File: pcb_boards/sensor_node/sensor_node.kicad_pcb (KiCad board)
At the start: 2 copper layers, 93 x 93 mm, 61 parts, among them IC1 PCF2129AT, J2 Conn_02x03_Odd_Even, J3 USB_B_Micro, U1 SiP32431, U2 ESP32-WROOM-32, U3 RF-LORA-868-SO, U7 RP604x, U8 SiP32431

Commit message: Merge with local version. Bug fixes and node improvements.
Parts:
- IC1: value PCF2129AT -> PCF2129T
- moved I2C2 1.00 mm to (67.5, 124.5)
- moved I2C3 1.00 mm to (102.5, 124.5)
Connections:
- net /~RST renamed /~{RST}
- net /~RST_I2C renamed /~{RST_I2C}
- net /~RST_RF renamed /~{RST_RF}
- IC1 pad 10: Net-(IC1-Pad10) -> unconnected-(IC1-Pad10)
- IC1 pad 11: Net-(IC1-Pad11) -> unconnected-(IC1-Pad11)
- IC1 pad 12: Net-(IC1-Pad12) -> unconnected-(IC1-Pad12)
- IC1 pad 13: Net-(IC1-Pad13) -> unconnected-(IC1-Pad13)
- IC1 pad 14: Net-(IC1-Pad14) -> unconnected-(IC1-Pad14)
- IC1 pad 15: Net-(IC1-Pad15) -> unconnected-(IC1-Pad15)
- IC1 pad 16: Net-(IC1-Pad16) -> unconnected-(IC1-Pad16)
- IC1 pad 3: Net-(IC1-Pad3) -> unconnected-(IC1-Pad3)
- IC1 pad 6: Net-(IC1-Pad6) -> unconnected-(IC1-Pad6)
- IC1 pad 7: Net-(IC1-Pad7) -> unconnected-(IC1-Pad7)
- IC1 pad 9: Net-(IC1-Pad9) -> unconnected-(IC1-Pad9)
- J3 pad 4: Net-(J3-Pad4) -> unconnected-(J3-Pad4)
- U1 pad 6: Net-(U1-Pad6) -> unconnected-(U1-Pad6)
- U2 pad 13: Net-(U2-Pad13) -> unconnected-(U2-Pad13)
- U2 pad 14: Net-(U2-Pad14) -> unconnected-(U2-Pad14)
- U2 pad 17: Net-(U2-Pad17) -> unconnected-(U2-Pad17)
- U2 pad 18: Net-(U2-Pad18) -> unconnected-(U2-Pad18)
- U2 pad 19: Net-(U2-Pad19) -> unconnected-(U2-Pad19)
- U2 pad 20: Net-(U2-Pad20) -> unconnected-(U2-Pad20)
- U2 pad 21: Net-(U2-Pad21) -> unconnected-(U2-Pad21)
- U2 pad 22: Net-(U2-Pad22) -> unconnected-(U2-Pad22)
- U2 pad 23: Net-(U2-Pad23) -> unconnected-(U2-Pad23)
- U2 pad 29: Net-(U2-Pad29) -> unconnected-(U2-Pad29)
- U2 pad 32: Net-(U2-Pad32) -> unconnected-(U2-Pad32)
- U3 pad 10: Net-(U3-Pad10) -> unconnected-(U3-Pad10)
- U3 pad 11: Net-(U3-Pad11) -> unconnected-(U3-Pad11)
- U3 pad 8: Net-(U3-Pad8) -> unconnected-(U3-Pad8)
- U3 pad 9: Net-(U3-Pad9) -> unconnected-(U3-Pad9)
- U8 pad 6: Net-(U8-Pad6) -> unconnected-(U8-Pad6)
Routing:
- net /SCL: track 163.8 -> 162.1 mm
- net /~{RST}: track 36.3 -> 37.6 mm
- net /SDA: track 144.9 -> 143.6 mm
- net /~{RST_I2C}: track 132.4 -> 131.7 mm
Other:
- net class Default removed
- net class Power removed
- board text added: "MIRRA"
- board text added: "RST"
- board text added: "Rev. 6"
- board text added: "~{RST}"
- board text removed: "GEMS"
- board text removed: "Rev. 5"
- board text removed: "~RST"

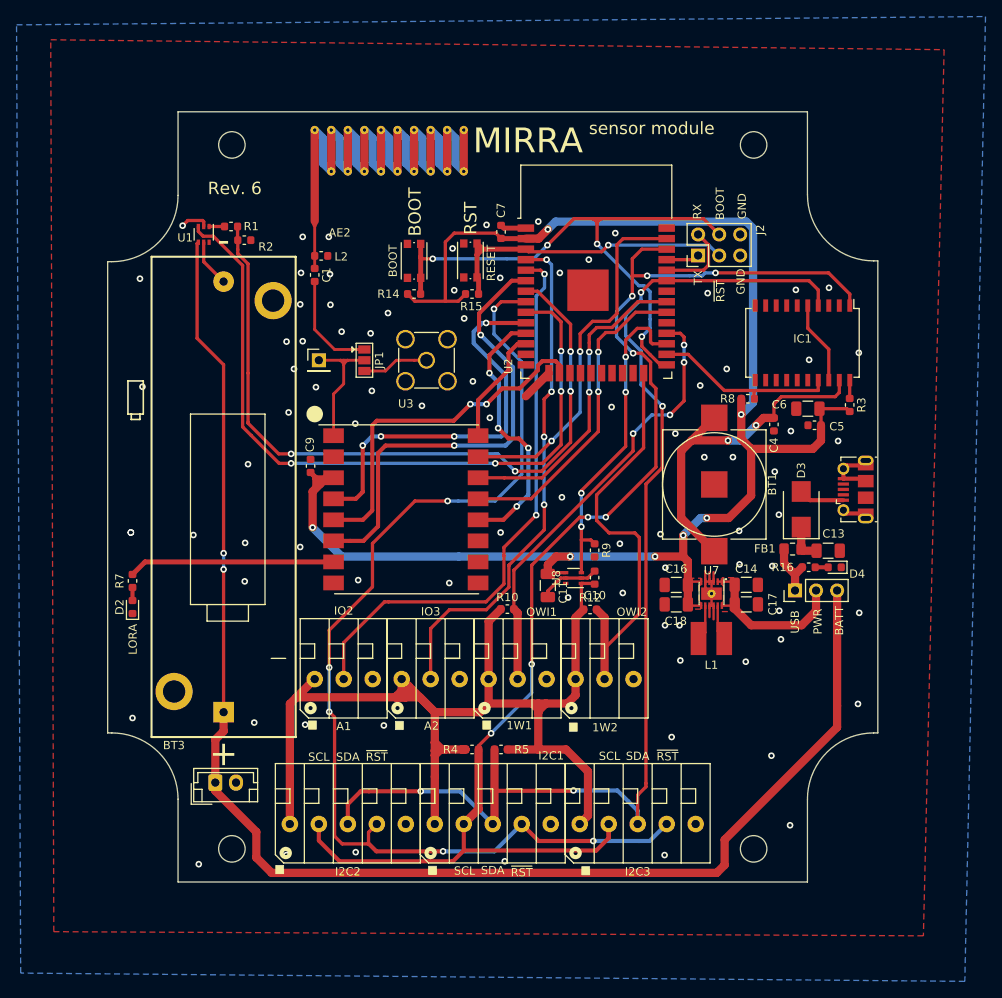
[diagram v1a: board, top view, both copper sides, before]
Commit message: New PDB version.
sensor node: added FTDI chip for USB comms
sensor node: implemented page feedback
sensor node: remove aerial, and SMA connector, update interfacing and RTC

sensor hat: update to two PCBs for reduced thermal conductivity
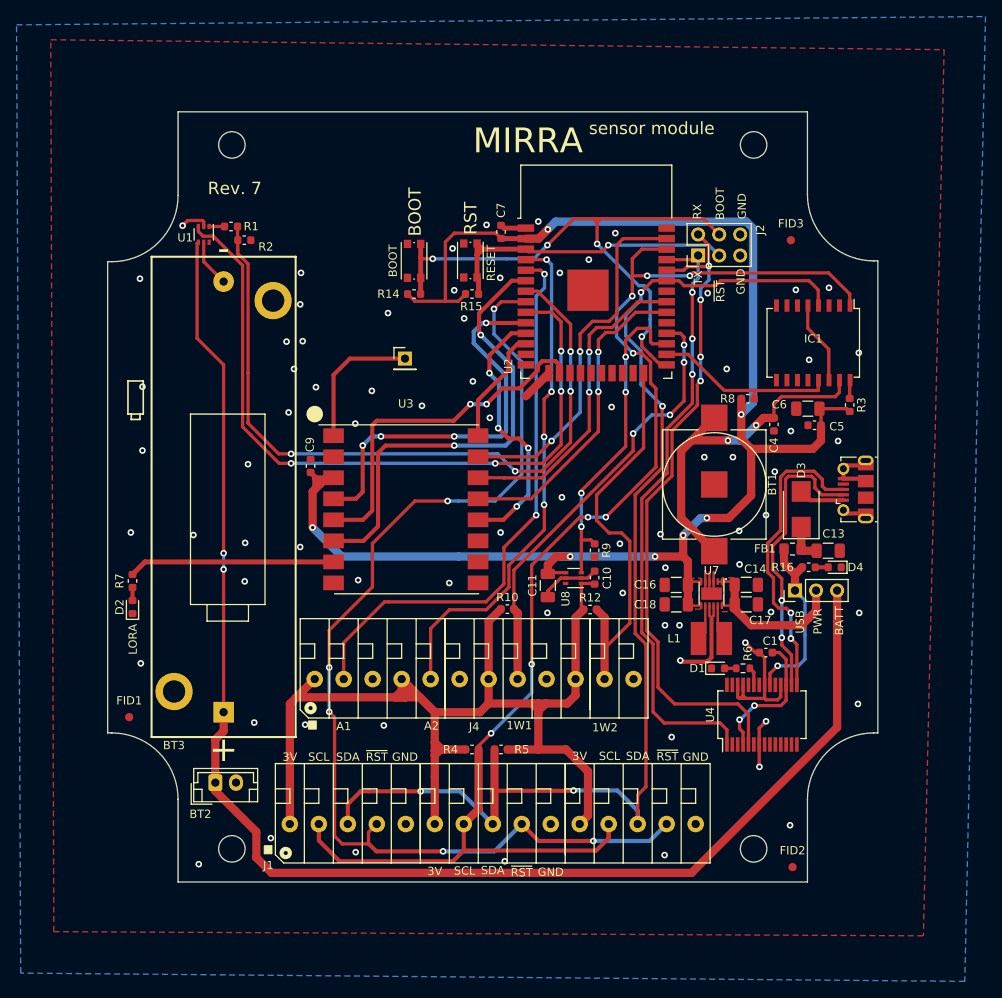
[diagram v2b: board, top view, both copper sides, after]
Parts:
- removed AE2: Antenna, RF_Antenna:Texas_SWRA416_868MHz_915MHz
- removed ANT1: Conn_Coaxial, Connector_Coaxial:SMA_Amphenol_901-144_Vertical
- removed I2C1, I2C2, I2C3: Conn_01x05, gems_footprints:TerminalBlock_Phoenix_PTSA-1,2-2-3,5-F-THR-1x05-P3.50mm_45Degree
- removed IO2, IO3, OWI1, OWI2: Conn_01x03, gems_footprints:TerminalBlock_Phoenix_PTSA-1,2-2-3,5-F-THR-1x03-P3.50mm_45Degree
- removed JP1: Jumper_3_Open, Jumper:SolderJumper-3_P1.3mm_Open_Pad1.0x1.5mm
- removed L2: 12nH, Inductor_SMD:L_0603_1608Metric
- added D1: LED, LED_SMD:LED_0603_1608Metric, F.Cu at (112.2, 105.7)
- added FID1: Fiducial, Fiducial:Fiducial_1mm_Mask2mm, F.Cu at (41.1, 111.6)
- added FID2: Fiducial, Fiducial:Fiducial_1mm_Mask2mm, F.Cu at (121.2, 129.7)
- added FID3: Fiducial, Fiducial:Fiducial_1mm_Mask2mm, F.Cu at (121.0, 54.0)
- added J1: Screw_Terminal_01x15, gems_footprints:TerminalBlock_Phoenix_PTSA-1,2-2-3,5-F-THR-1x15-P3.50mm_45Degree, F.Cu at (85.0, 124.5)
- added J4: Screw_Terminal_01x12, gems_footprints:TerminalBlock_Phoenix_PTSA-1,2-2-3,5-F-THR-1x12-P3.50mm_45Degree, F.Cu at (82.8, 107.0)
- added R6: 60R, Resistor_SMD:R_0603_1608Metric, F.Cu at (115.2, 105.7)
- added U4: FT232RL, Package_SO:SSOP-28_5.3x10.2mm_P0.65mm, F.Cu at (117.5, 111.3)
- C1: value 1pF -> 100nF
- IC1: footprint gems_footprints:SO20 -> gems_footprints:SO16
- moved C1 71.0 mm to (118.0, 103.8), turned to 180 degrees
- moved AE1 10.4 mm to (74.4, 68.3)
- moved IC1 1.30 mm to (123.7, 66.4)
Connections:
- net +3V3 renamed +3.3V
- C1 pad 2: Net-(C1-Pad2) -> GND
- IC1 pad 13: unconnected-(IC1-Pad13) -> /INT_T
- IC1 pad 14: unconnected-(IC1-Pad14) -> /BBS
- IC1 pad 15: unconnected-(IC1-Pad15) -> Net-(BT1-Pad1)
- IC1 pad 16: unconnected-(IC1-Pad16) -> Net-(IC1-Pad16)
- R3 pad 1: Net-(IC1-Pad20) -> Net-(IC1-Pad16)
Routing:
- net /RX: track 9.53 -> 80.1 mm, vias 0 -> 4
- net /TX: track 4.01 -> 74.1 mm, vias 0 -> 3
- net /D+: track 0.00 -> 37.0 mm, vias 0 -> 2
- net /D-: track 0.00 -> 35.1 mm, vias 0 -> 2
- net GND: track 46.7 -> 77.2 mm, vias 86 -> 77
- net VBUS: track 6.82 -> 21.9 mm, vias 0 -> 1
- net Net-(C1-Pad2): track 12.8 -> 0.00 mm
- net Net-(C1-Pad1): track 4.84 -> 16.7 mm, vias 0 -> 2
- net Net-(ANT1-Pad1): track 8.04 -> 0.00 mm
- net Net-(IC1-Pad20): track 2.22 -> 0.00 mm
- net Net-(IC1-Pad16): track 0.00 -> 2.22 mm
- net Net-(R6-Pad1): track 0.00 -> 2.20 mm
- net /ONE_W2: track 53.8 -> 51.9 mm
- net +BATT: track 174.8 -> 173.0 mm
- net /SDA: track 143.6 -> 145.2 mm
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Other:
- board text added: "3V"
- board text added: "Rev. 7"
- board text removed: "Rev. 6"
